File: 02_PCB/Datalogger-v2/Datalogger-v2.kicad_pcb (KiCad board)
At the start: 2 copper layers, 112.9 x 90 mm, 25 parts, among them U1 Micro SD Card Adapter, U7 TP4056, U8 ESP32 DEV KIT DOIT

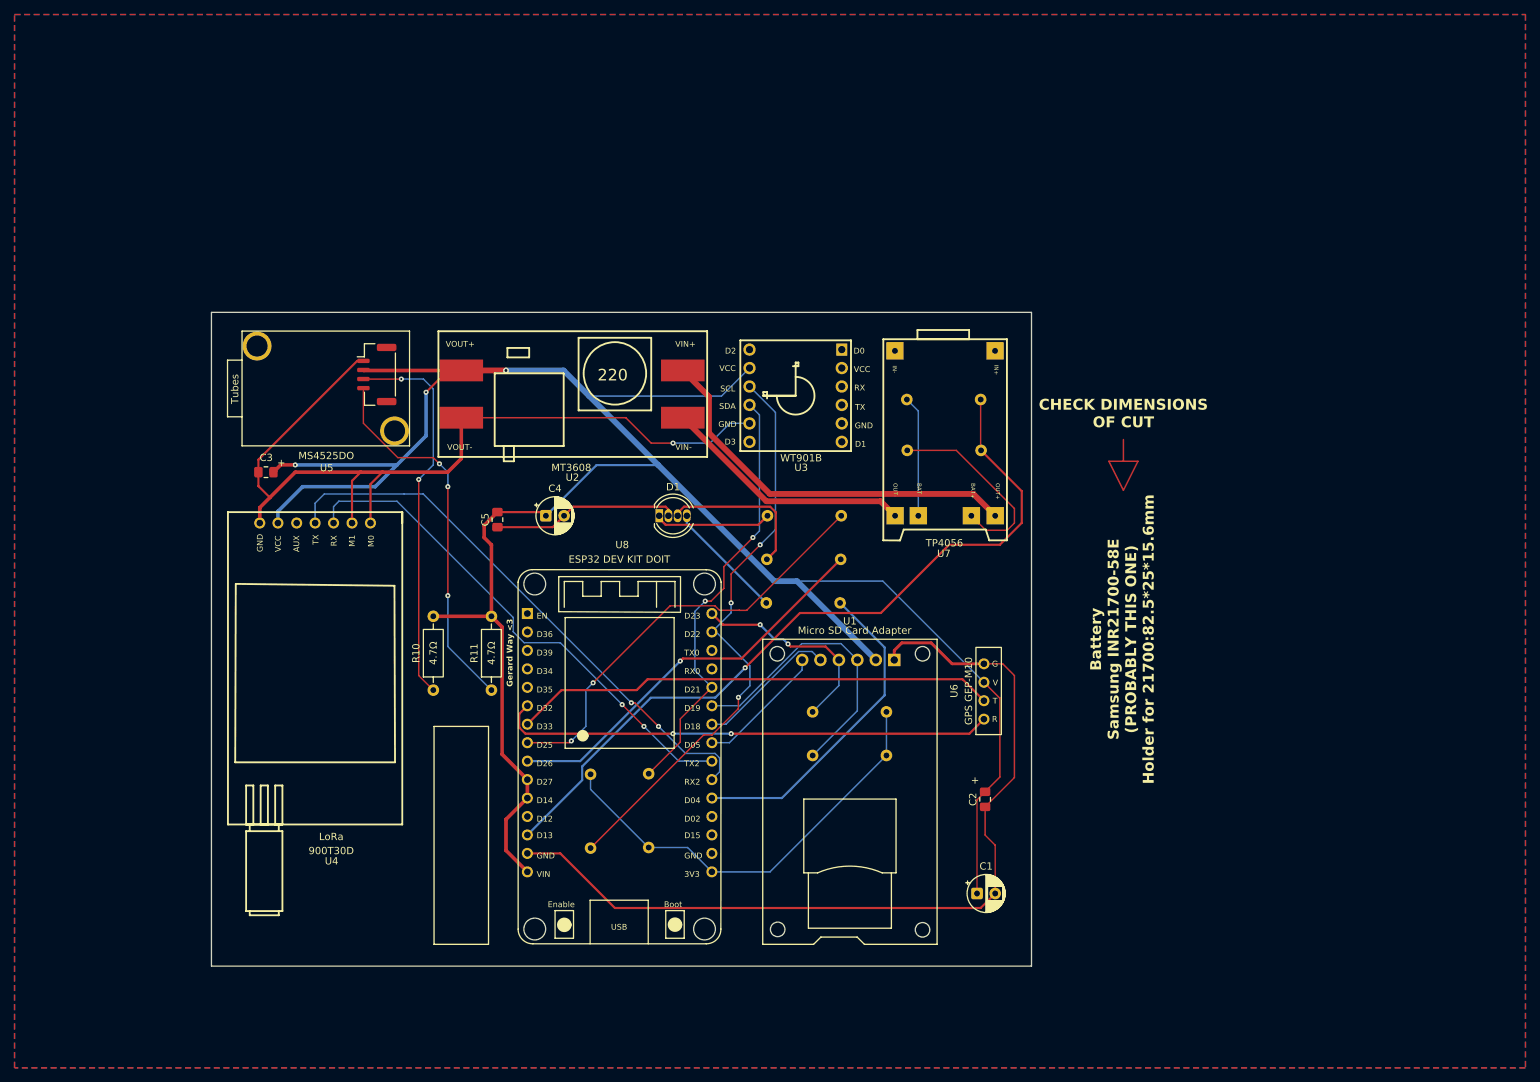
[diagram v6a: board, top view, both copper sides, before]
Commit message: Update PCB layout and schematic
- Removed Step-Up Converter and Battery Charger
- Added button
- Fixed errors
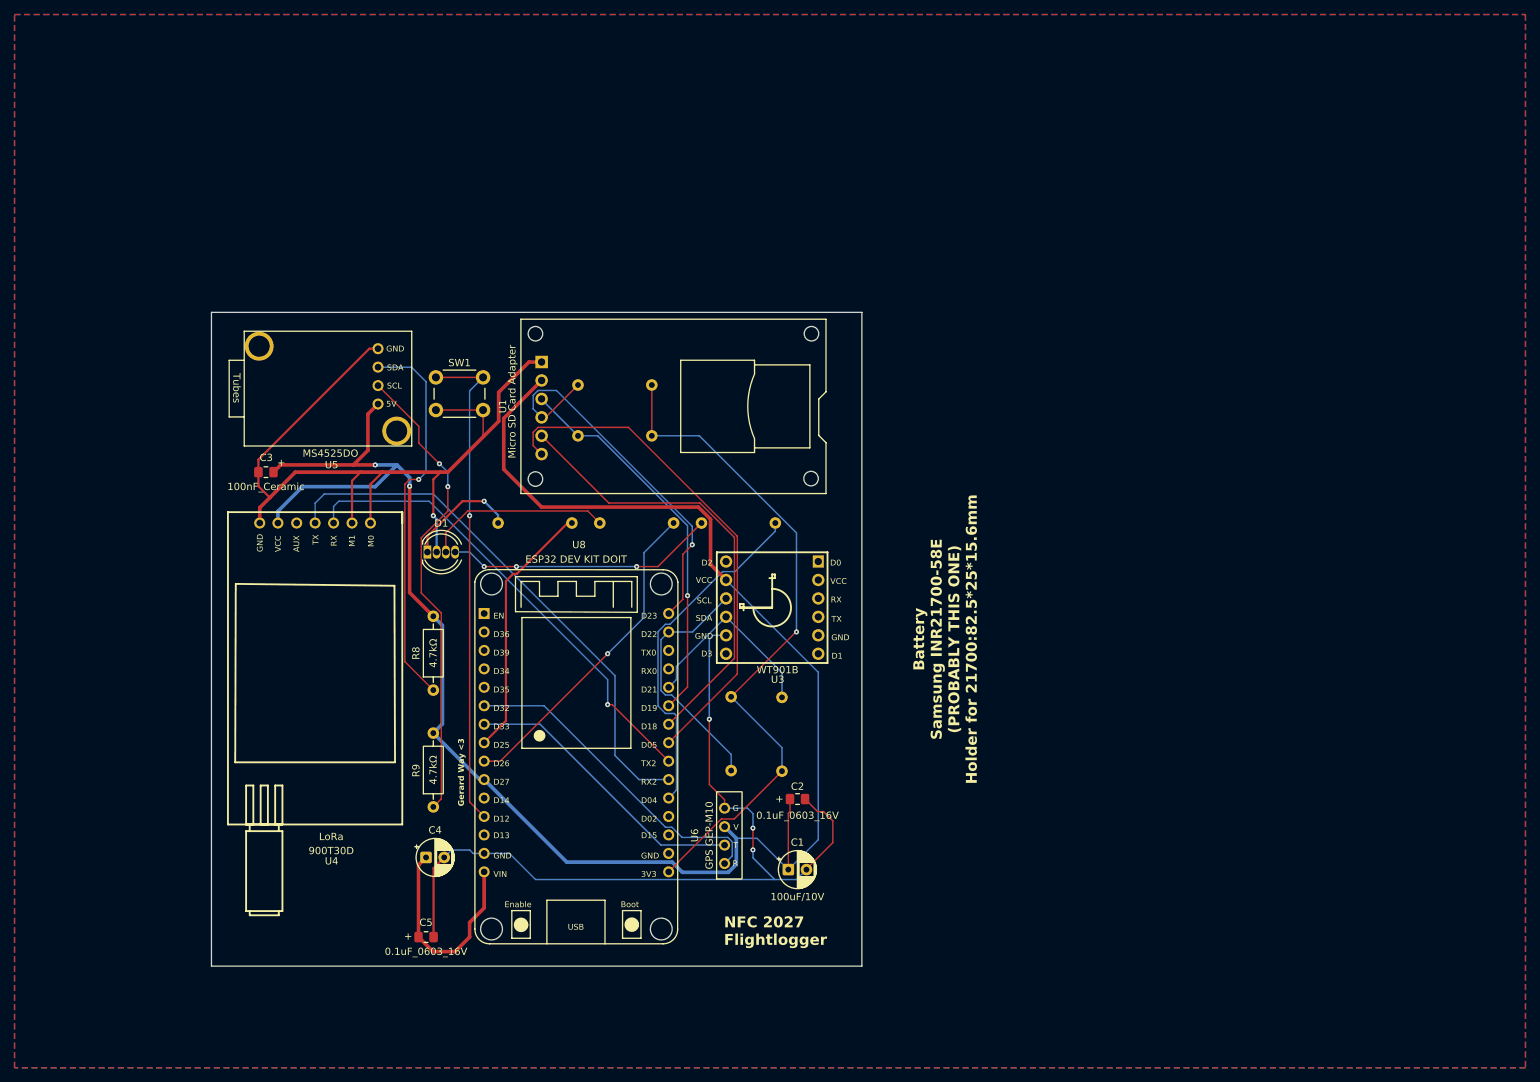
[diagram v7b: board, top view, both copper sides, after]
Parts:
- removed the R3 at (174.3, 72.0)
- removed the R4 at (174.4, 79.0)
- removed U2: ~, Datalogger-v2:MT3608
- removed U7: TP4056, Datalogger-v2:TP4056
- added SW1: SW_Push, Button_Switch_THT:SW_PUSH_6mm, F.Cu at (99.4, 69.0)
- R2: value 4.7Ω -> 4.7kΩ
- R8: renamed from R10; value 4.7Ω -> 4.7kΩ
- R9: renamed from R11; value 4.7Ω -> 4.7kΩ
- moved U1 62.7 mm to (153.1, 84.9), turned to 180 degrees
- moved C5 58.3 mm to (98.0, 146.0), turned to 180 degrees
- moved R6 55.4 mm to (129.1, 70.0)
- moved R7 54.6 mm to (129.1, 77.0)
- moved C4 49.8 mm to (98.0, 135.0)
- moved U6 40.9 mm to (140.0, 132.0)
- moved R5 37.1 mm to (118.1, 89.0)
- moved D1 32.3 mm to (98.2, 93.0)
- moved U3 29.4 mm to (145.5, 100.7)
- moved U5 29.0 mm to (84.3, 56.0), turned to 0 degrees
- moved C1 26.2 mm to (147.9, 136.7)
- moved C2 25.8 mm to (149.1, 127.0), turned to 180 degrees
- moved R4 23.5 mm to (132.1, 89.0)
- moved R2 22.1 mm to (140.0, 123.1)
- moved R1 21.1 mm to (147.0, 123.2)
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- renumbered R5 to R3, R6 to R4, R7 to R5, R8 to R6, R9 to R7
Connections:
- U5 pad 2: +5V -> Net-(U5-SDA)
- U5 pad 3: Net-(U5-SDA) -> Net-(U5-SCL)
- U5 pad 4: Net-(U5-SCL) -> +5V
- U8 pad 12: unconnected-(U8-ADC/D12-Pad12) -> Net-(U8-ADC/D12)
- U8 pad 13: Net-(U8-ADC/D13) -> unconnected-(U8-ADC/D13-Pad13)
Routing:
- net Net-(U8-ADC/D13): track 106.3 -> 0.00 mm, vias 1 -> 0
- net Net-(U8-ADC/D12): track 0.00 -> 68.5 mm, vias 0 -> 1
- net Net-(U2-VIN+): track 54.2 -> 0.00 mm
- net Net-(U1-CS): track 18.0 -> 70.4 mm
- net Net-(U3-SCL): track 80.9 -> 33.9 mm, vias 3 -> 0
- net Net-(U1-SCK): track 19.6 -> 61.8 mm
- net Net-(U2-VIN-): track 34.8 -> 0.00 mm
- net +3.3V: track 60.1 -> 93.3 mm, vias 0 -> 1
- net GND: track 268.8 -> 235.7 mm, vias 1 -> 4
- net Net-(U3-SDA): track 60.1 -> 27.2 mm, vias 2 -> 0
- net Net-(BT1-+): track 27.2 -> 0.00 mm
- net Net-(U6-TX): track 66.6 -> 40.0 mm
- net Net-(U1-MOSI): track 28.8 -> 53.6 mm, vias 2 -> 1
- net Net-(U8-ADC/DAC0/D25): track 59.6 -> 35.9 mm, vias 2 -> 0
- net +5V: track 317.9 -> 294.6 mm, vias 3 -> 2
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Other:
- board size 112.9 x 90 mm -> 89.5 x 90 mm
- board text added: "NFC 2027 Flightlogger"
- board text added: "Now for real. No rick-roll."
- board text removed: "CHECK DIMENSIONS OF CUT"

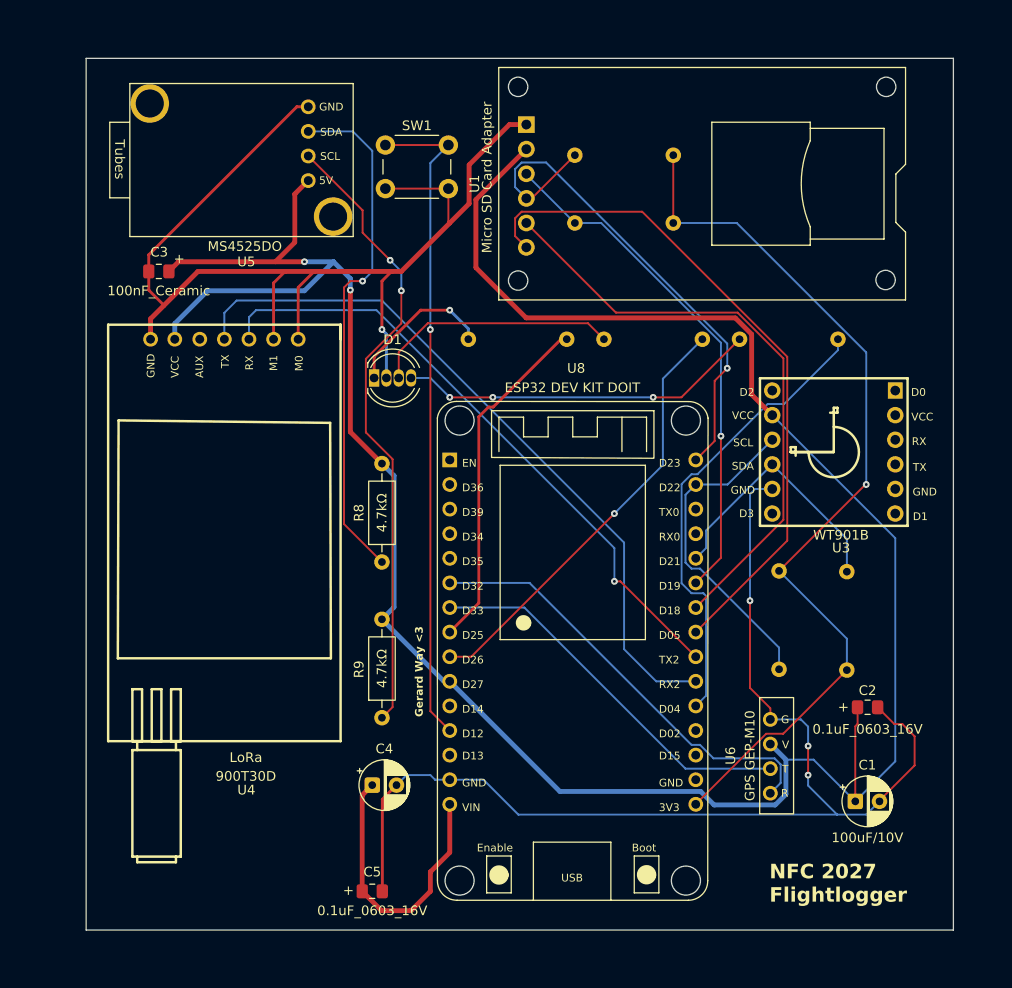
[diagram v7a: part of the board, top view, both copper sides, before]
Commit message: Update PCB layout
- Change SD Card Reader layer
- Add holes for soft mount
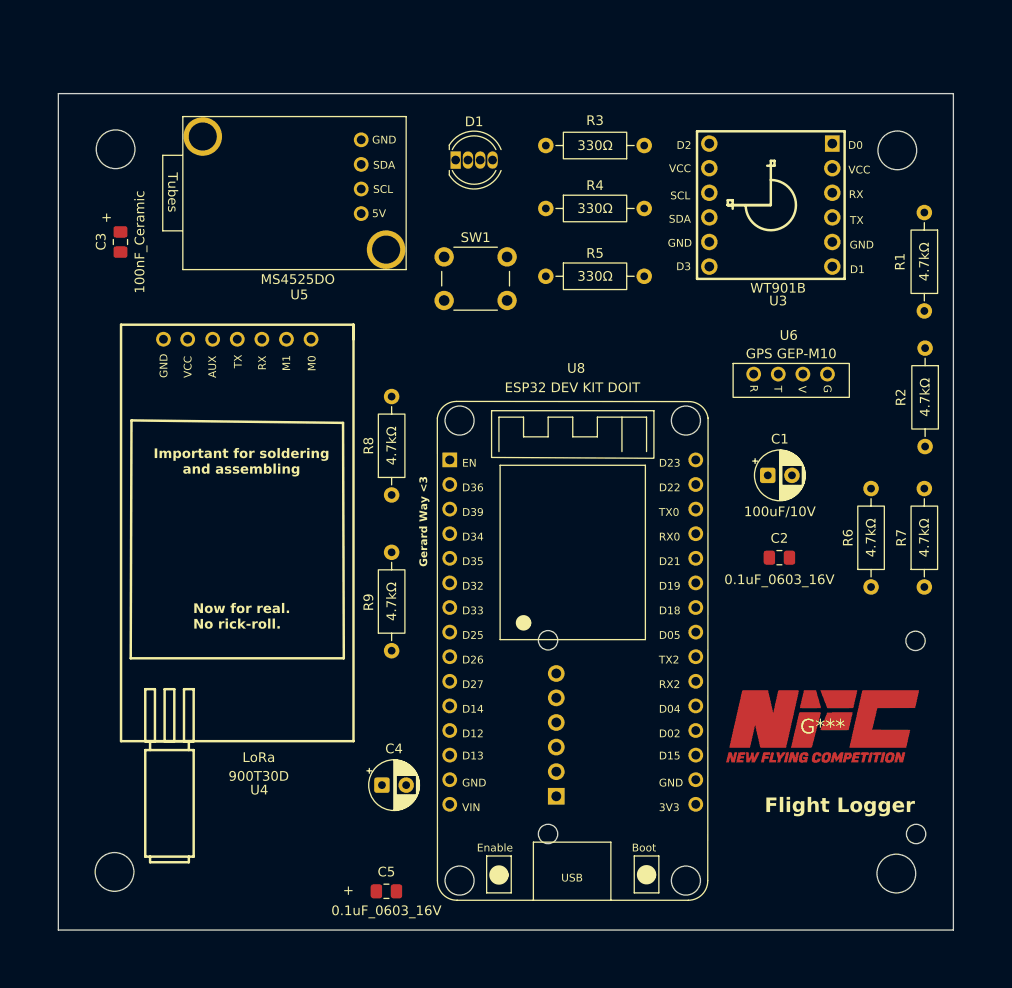
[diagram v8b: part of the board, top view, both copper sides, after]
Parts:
- added ?: , , F.Cu at (71.5, 69.4)
- added ?: , , F.Cu at (152.2, 69.5)
- added ?: , , F.Cu at (71.4, 144.0)
- added ?: , , F.Cu at (152.1, 144.2)
- added G***: LOGO, LOGO, F.Cu at (144.5, 129.0)
- R1, R2, R3, R4, R5, R6, R7: moved to F.Cu
- U1: moved to B.Cu
- moved R6 49.0 mm to (149.5, 114.6), turned to 90 degrees
- moved R1 47.9 mm to (155.0, 75.9), turned to -90 degrees
- moved R7 45.7 mm to (155.0, 114.6), turned to 90 degrees
- moved U6 38.5 mm to (141.3, 93.5), turned to 0 degrees
- moved R2 36.4 mm to (155.1, 89.9), turned to -90 degrees
- moved C1 34.8 mm to (138.8, 103.1)
- moved U1 33.3 mm to (156.2, 118.1)
- moved R3 28.3 mm to (126.1, 69.0)
- moved U3 26.3 mm to (139.0, 75.2)
- moved D1 24.0 mm to (106.6, 70.5)
- moved R4 21.1 mm to (115.9, 75.5), turned to 0 degrees
- moved C2 17.9 mm to (140.0, 111.6)
- moved SW1 13.0 mm to (105.4, 80.5)
- moved R9 6.99 mm to (100.0, 121.2)
- moved R8 6.99 mm to (100.0, 105.1)
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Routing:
- net +5V: track 294.6 -> 0.00 mm, vias 2 -> 0
- net GND: track 235.7 -> 0.00 mm, vias 4 -> 0
- net +3.3V: track 93.3 -> 0.00 mm, vias 1 -> 0
- net Net-(U4-TX): track 74.7 -> 0.00 mm
- net Net-(U1-CS): track 70.4 -> 0.00 mm
- net Net-(U8-ADC/D12): track 68.5 -> 0.00 mm, vias 1 -> 0
- net Net-(U4-RX): track 65.5 -> 0.00 mm, vias 1 -> 0
- net Net-(U5-SCL): track 65.1 -> 0.00 mm, vias 2 -> 0
- net Net-(U1-SCK): track 61.8 -> 0.00 mm
- net Net-(U1-MOSI): track 53.6 -> 0.00 mm, vias 1 -> 0
- net Net-(U5-SDA): track 53.5 -> 0.00 mm, vias 1 -> 0
- net Net-(U1-MISO): track 53.2 -> 0.00 mm, vias 1 -> 0
- net Net-(U8-ADC/D4): track 48.1 -> 0.00 mm
- net Net-(U6-RX): track 45.3 -> 0.00 mm
- net Net-(U8-ADC/DAC1/D26): track 44.9 -> 0.00 mm, vias 1 -> 0
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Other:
- board size 89.5 x 90 mm -> 92.4 x 86.4 mm
- board text added: "Flight Logger"
- board text removed: "NFC 2027 Flightlogger"
